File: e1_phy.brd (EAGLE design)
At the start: 100 x 75 mm, 138 parts, among them IC2 LD117AS33TR, IC3 LD117AS33TR, IC4 MAX6173AASA, U1 IDT82V2081, U2 GPS_GNS_2201, U3 VCTCXO-CONNORWINFIELD, U4 VCXO_TAITIEN_VT, U5 IP4234CZ6, U7 IP4234CZ6, X1 BU-SMA-G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

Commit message: Testpads for unused LIU signals.
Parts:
- added R29: 10k, rcl:R0603
- added TP1, TP2, TP3: TPB1,27, testpad:B1,27
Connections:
- new net N$4: TP2.TP, U1.6
- new net N$6: R29.2, TP1.TP, U1.3
- new net N$8: TP3.TP, U1.7
- net GND: now also R29.1; no longer U1.3
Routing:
- net N$6: track 0.00 -> 12.1 mm
- net N$8: track 0.00 -> 2.90 mm
- net N$4: track 0.00 -> 1.82 mm
- net GND: vias 152 -> 154
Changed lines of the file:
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@@
 <dimension x1="100" y1="0" x2="100" y2="1" x3="110" y3="0.5" textsize="1.27" layer="47"/>
 <text x="18.0975" y="1.74625" size="0.6096" layer="25" font="vector">RxCtr TxCtr</text>
-<text x="64.77" y="71.12" size="0.6096" layer="25" font="vector">e1_sam4_usb</text>
+<text x="82.55" y="66.51625" size="0.6096" layer="25" font="vector">e1_sam4_usb</text>
 <text x="87.3125" y="69.85" size="1.778" layer="1" font="vector" ratio="12">Top</text>
 <text x="91.59875" y="69.85" size="1.778" layer="16" font="vector" ratio="12" rot="MR0">Bot</text>
-<text x="64.77" y="68.58" size="0.6096" layer="25" font="vector">vogelchr@vogel.cx
+<text x="82.55" y="64.77" size="0.6096" layer="25" font="vector">vogelchr@vogel.cx
 2018-07-03 for review</text>
 <text x="36.83" y="71.12" size="1.6764" layer="1" font="vector" ratio="20">osmocom e1 usb interface</text>
@@
 <attribute name="SPICEPREFIX" value="R" x="63.8175" y="55.88" size="1.778" layer="27" display="off"/>
 </element>
+<element name="TP1" library="testpad" library_urn="urn:adsk.eagle:library:385" package="B1,27" package3d_urn="urn:adsk.eagle:package:27944/1" value="TPB1,27" x="63.5" y="6.35">
+<attribute name="TP_SIGNAL_NAME" value="" x="63.5" y="6.35" size="1.778" layer="27" display="off"/>
+</element>
+<element name="TP2" library="testpad" library_urn="urn:adsk.eagle:library:385" package="B1,27" package3d_urn="urn:adsk.eagle:package:27944/1" value="TPB1,27" x="67.31" y="6.35">
+<attribute name="TP_SIGNAL_NAME" value="" x="67.31" y="6.35" size="1.778" layer="27" display="off"/>
+</element>
+<element name="R29" library="rcl" library_urn="urn:adsk.eagle:library:334" package="R0603" package3d_urn="urn:adsk.eagle:package:23555/2" value="10k" x="55.88" y="7.62" rot="R270">
+<attribute name="SPICEPREFIX" value="R" x="55.88" y="7.62" size="1.778" layer="27" rot="R270" display="off"/>
+</element>
+<element name="TP3" library="testpad" library_urn="urn:adsk.eagle:library:385" package="B1,27" package3d_urn="urn:adsk.eagle:package:27944/1" value="TPB1,27" x="68.42125" y="5.3975">
+<attribute name="TP_SIGNAL_NAME" value="" x="68.42125" y="5.3975" size="1.778" layer="27" display="off"/>
+</element>
 </elements>
 <signals>
@@
 <contactref element="U1" pad="17"/>
 <contactref element="U1" pad="11"/>
-<contactref element="U1" pad="3"/>
 <contactref element="U1" pad="22"/>
 <contactref element="U1" pad="15"/>
@@
 <via x="63.02375" y="14.44625" extent="1-16" drill="0.35"/>
 <via x="67.945" y="11.7475" extent="1-16" drill="0.35"/>
-<via x="64.92875" y="6.82625" extent="1-16" drill="0.35"/>
+<via x="65.7225" y="6.82625" extent="1-16" drill="0.35"/>
 <via x="72.7075" y="8.5725" extent="1-16" drill="0.35"/>
-<via x="64.92875" y="4.92125" extent="1-16" drill="0.35"/>
+<via x="65.7225" y="4.92125" extent="1-16" drill="0.35"/>
 <via x="54.9275" y="9.525" extent="1-16" drill="0.35"/>
 <via x="53.34" y="4.92125" extent="1-16" drill="0.35"/>
@@
 <via x="78.105" y="7.62" extent="1-16" drill="0.35"/>
 <via x="71.59625" y="11.7475" extent="1-16" drill="0.35"/>
-<via x="59.69" y="7.77875" extent="1-16" drill="0.35"/>
-<via x="54.9275" y="7.62" extent="1-16" drill="0.35"/>
-<via x="64.92875" y="3.81" extent="1-16" drill="0.35"/>
+<via x="59.69" y="8.255" extent="1-16" drill="0.35"/>
+<via x="60.0075" y="9.68375" extent="1-16" drill="0.35"/>
+<via x="73.025" y="6.50875" extent="1-16" drill="0.35"/>
 <via x="81.12125" y="4.445" extent="1-16" drill="0.35"/>
 <via x="79.53375" y="5.08" extent="1-16" drill="0.35"/>
@@
 <via x="61.595" y="56.515" extent="1-16" drill="0.35"/>
 <via x="61.595" y="55.245" extent="1-16" drill="0.35"/>
+<contactref element="R29" pad="1"/>
+<via x="59.69" y="6.82625" extent="1-16" drill="0.35"/>
+<via x="73.025" y="4.92125" extent="1-16" drill="0.35"/>
 </signal>
 <signal name="LINE_PIN1">
@@
 <wire x1="71.07375" y1="48.895" x2="70.7" y2="49.26875" width="0.1524" layer="1"/>
 </signal>
+<signal name="N$4">
+<contactref element="U1" pad="6"/>
+<contactref element="TP2" pad="TP"/>
+<wire x1="67.31" y1="8.17" x2="67.31" y2="6.35" width="0.1524" layer="1"/>
+</signal>
+<signal name="N$6">
+<contactref element="U1" pad="3"/>
+<contactref element="R29" pad="2"/>
+<contactref element="TP1" pad="TP"/>
+<wire x1="64.91" y1="8.17" x2="64.91" y2="6.49" width="0.1524" layer="1"/>
+<wire x1="64.91" y1="6.49" x2="64.77" y2="6.35" width="0.1524" layer="1"/>
+<wire x1="64.77" y1="6.35" x2="63.5" y2="6.35" width="0.1524" layer="1"/>
+<wire x1="63.5" y1="6.35" x2="62.23" y2="7.62" width="0.1524" layer="1"/>
+<wire x1="62.23" y1="7.62" x2="56.03875" y2="7.62" width="0.1524" layer="1"/>
+<wire x1="56.03875" y1="7.62" x2="55.88" y2="7.46125" width="0.1524" layer="1"/>
+<wire x1="55.88" y1="7.46125" x2="55.88" y2="6.77" width="0.1524" layer="1"/>
+</signal>
+<signal name="N$8">
+<contactref element="U1" pad="7"/>
+<contactref element="TP3" pad="TP"/>
+<wire x1="68.11" y1="8.17" x2="68.11" y2="6.82" width="0.1524" layer="1"/>
+<wire x1="68.11" y1="6.82" x2="68.42125" y2="6.50875" width="0.1524" layer="1"/>
+<wire x1="68.42125" y1="6.50875" x2="68.42125" y2="5.3975" width="0.1524" layer="1"/>
+</signal>
 </signals>

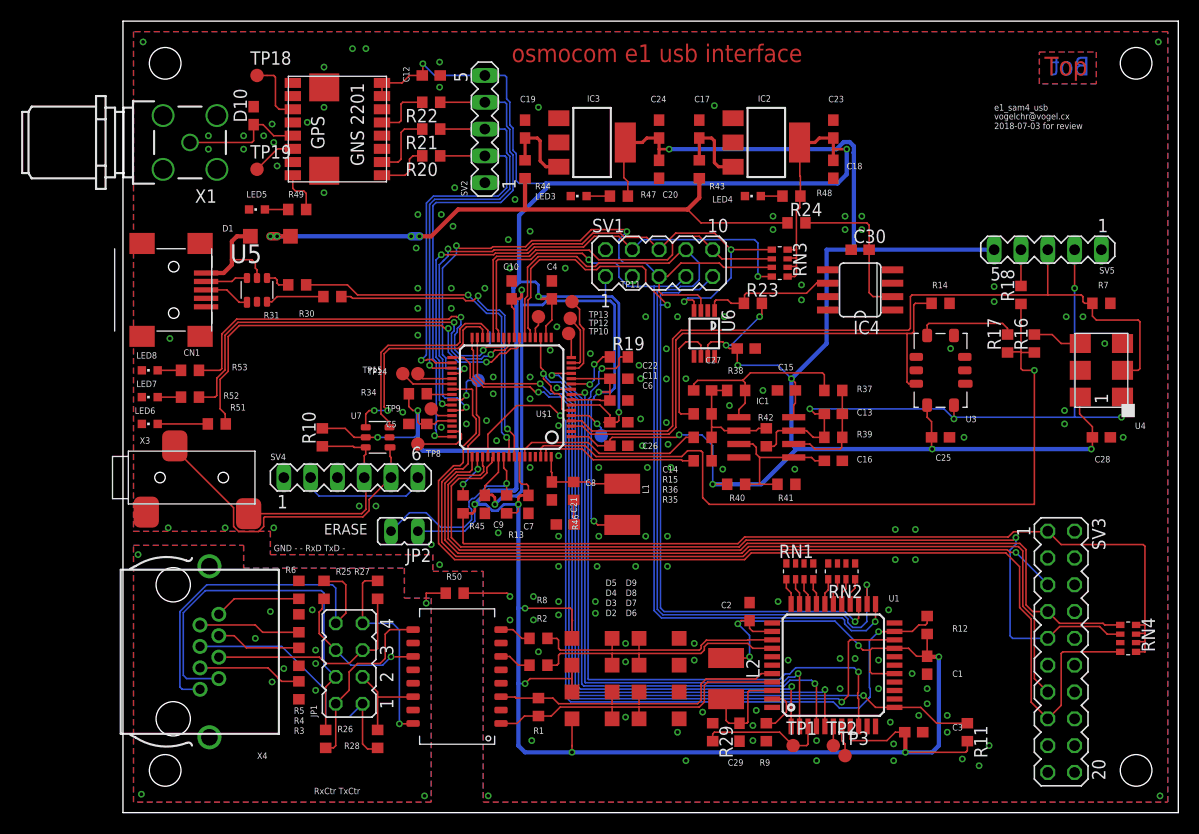
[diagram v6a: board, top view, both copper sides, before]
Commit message: Cleaned up silkscreen.
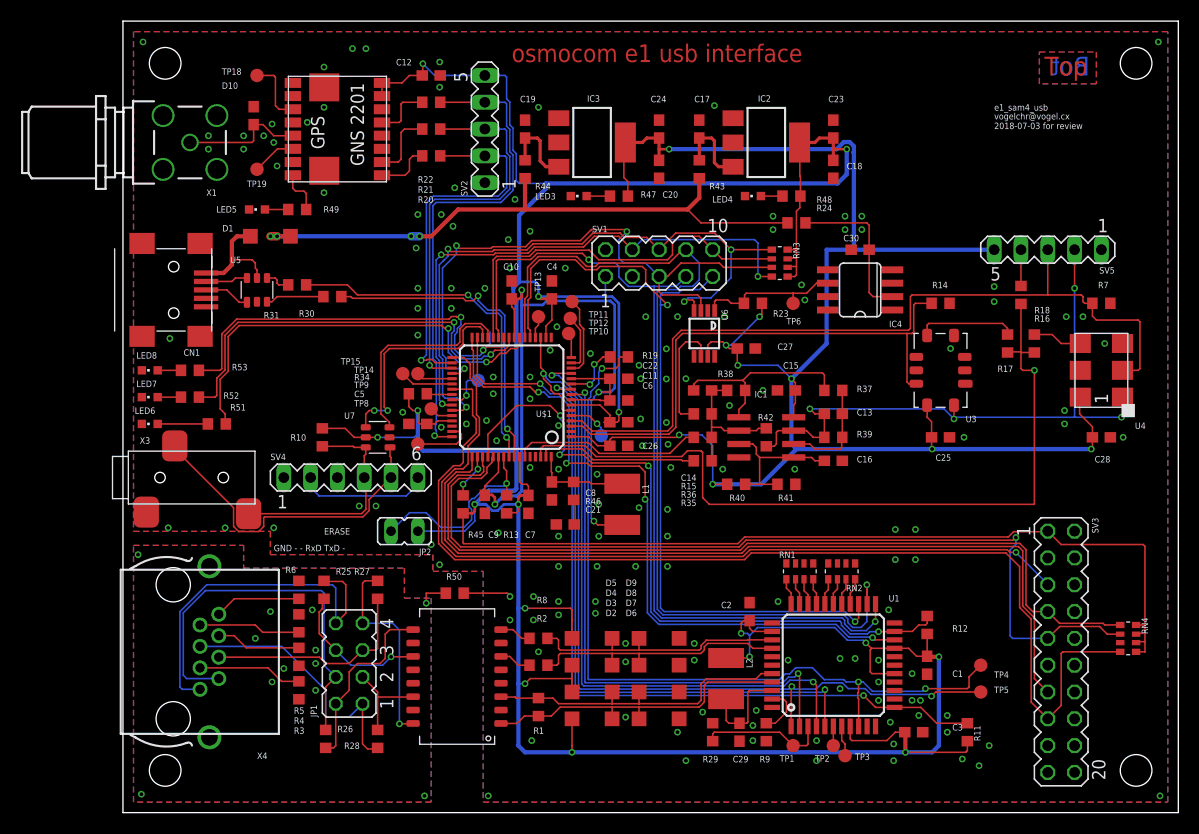
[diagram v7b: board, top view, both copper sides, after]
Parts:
- added TP4, TP5, TP6: TPB1,27, testpad:B1,27
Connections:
- net CLK2048: now also TP4.TP
- net N$7: now also TP6.TP
- net TX_CLK: now also TP5.TP
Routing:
- net TX_CLK: track 64.6 -> 83.6 mm, vias 2 -> 3
- net #SPI_CS1: track 79.3 -> 65.6 mm, vias 2 -> 4
- net CLK2048: track 64.8 -> 77.7 mm, vias 2 -> 3
- net #LIU_INT: track 78.0 -> 65.4 mm, vias 2 -> 4
- net VCC: track 432.6 -> 431.4 mm
- net N$7: track 13.0 -> 13.9 mm
- net GND: vias 154 -> 156
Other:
- board text removed: "RxCtr TxCtr"

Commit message: Some cleanup before declaring final.
ADVREF of SAM4S fed by VREF net.
+UB/2 divider fed by VREF net, renamed to VREF_HALF.
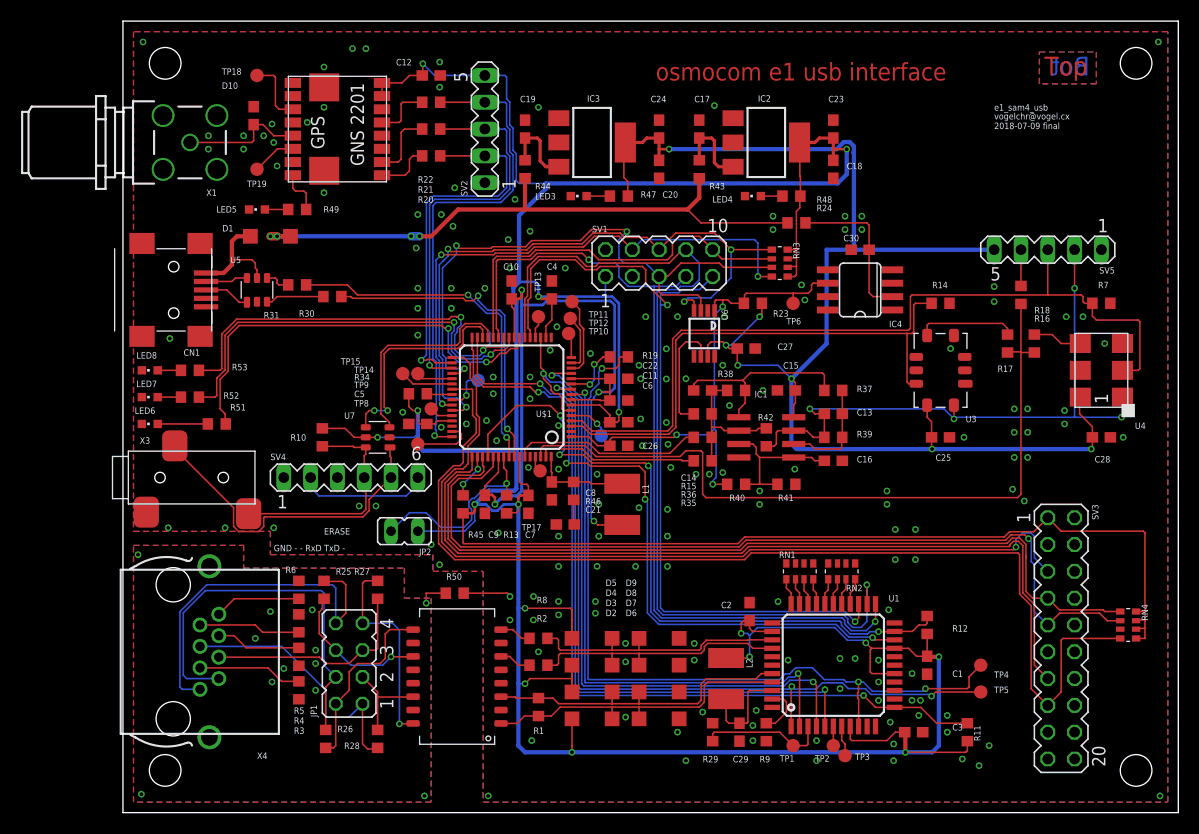
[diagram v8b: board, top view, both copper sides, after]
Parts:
- added TP17: TPB1,27, testpad:B1,27
- moved SV3 1.27 mm to (88.9, 16.5)
- moved RN4 1.27 mm to (95.2, 17.8)
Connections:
- net +UB_HALF renamed VREF_HALF
- removed net N$7: IC4.6, R23.1, TP6.TP, U6.1
- new net TP17: TP17.TP, U$1.61
- new net VREF: C26.2, IC4.6, R23.1, R40.1, TP6.TP, U$1.1, U6.1
- net +UB: no longer C26.2, R40.1, U$1.1
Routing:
- net VREF: track 0.00 -> 48.5 mm, vias 0 -> 3
- net +UB: track 163.9 -> 134.7 mm, vias 9 -> 7
- net N$7: track 13.9 -> 0.00 mm
- net SAM4S_CLK: track 75.7 -> 72.0 mm, vias 1 -> 0
- net TCK_SWDCLK: track 85.6 -> 82.8 mm
- net TDI: track 80.8 -> 83.2 mm
- net TP17: track 0.00 -> 1.52 mm
- net VCC: track 431.4 -> 432.0 mm
- net #RESET: track 102.9 -> 102.3 mm
- net TMS_SWDIO: track 81.1 -> 80.6 mm
- net TDO: track 79.8 -> 79.3 mm
- net GND: vias 156 -> 171
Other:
- board text added: "vogelchr@vogel.cx 2018-07-09 final"
- board text removed: "vogelchr@vogel.cx 2018-07-03 for review"
